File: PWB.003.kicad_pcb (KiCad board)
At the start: 2 copper layers, 61 x 31.5 mm, 58 parts, among them J1 USB_C_Receptacle_PowerOnly_6P, J2 XT30PW-F, J3 XT30PW-M, J4 BAT, J5 Conn_01x04_Pin, J6 Conn_01x05_Pin, Q1 IRLML6402TR, Q2 IRLML6402TR, Q3 2N7002, Q4 IRLML6402TR, U1 TPS63070RNMR, U2 BQ24073RGT

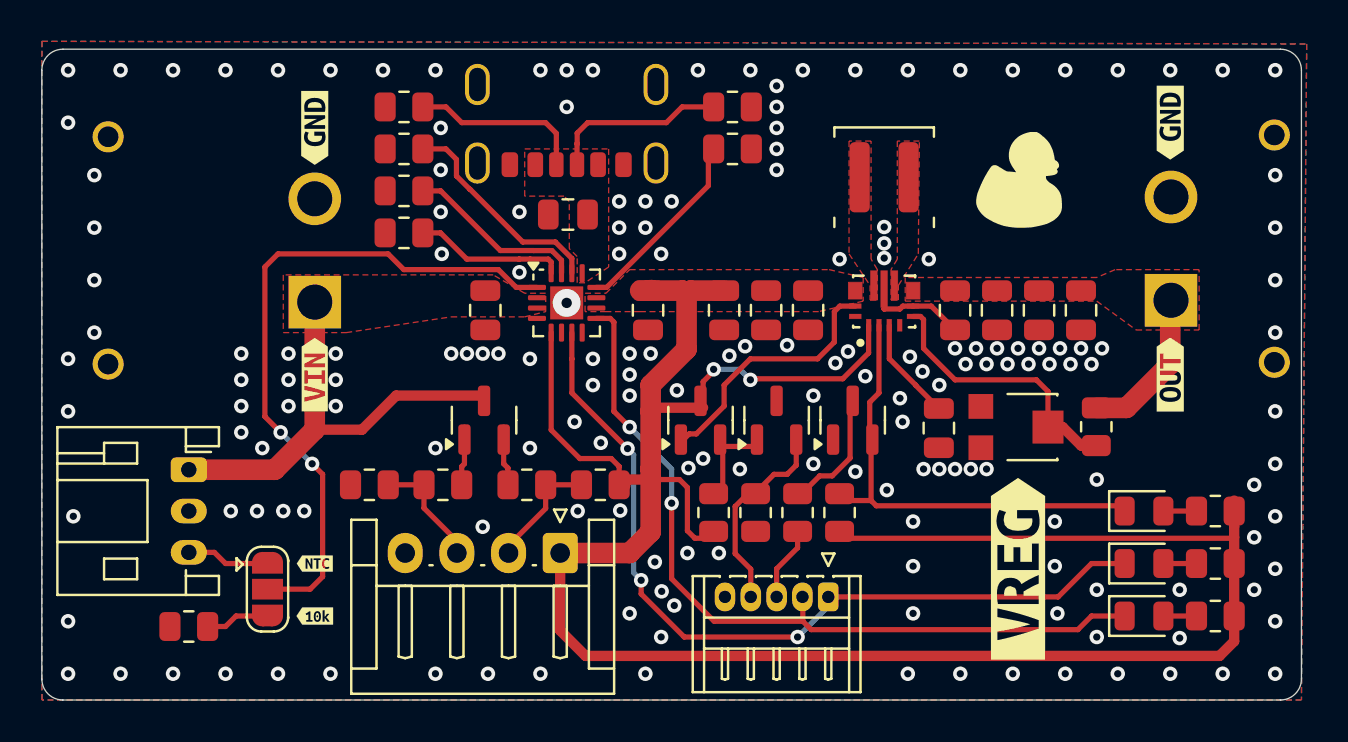
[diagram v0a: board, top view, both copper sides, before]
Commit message: Improved PCB
- Added 10k resistor on control inputs TPS63070
- Changed layout of inductor and filtering capacitors
- added legend on bottom layer
- updated DRC
- validated design on JLCDFM
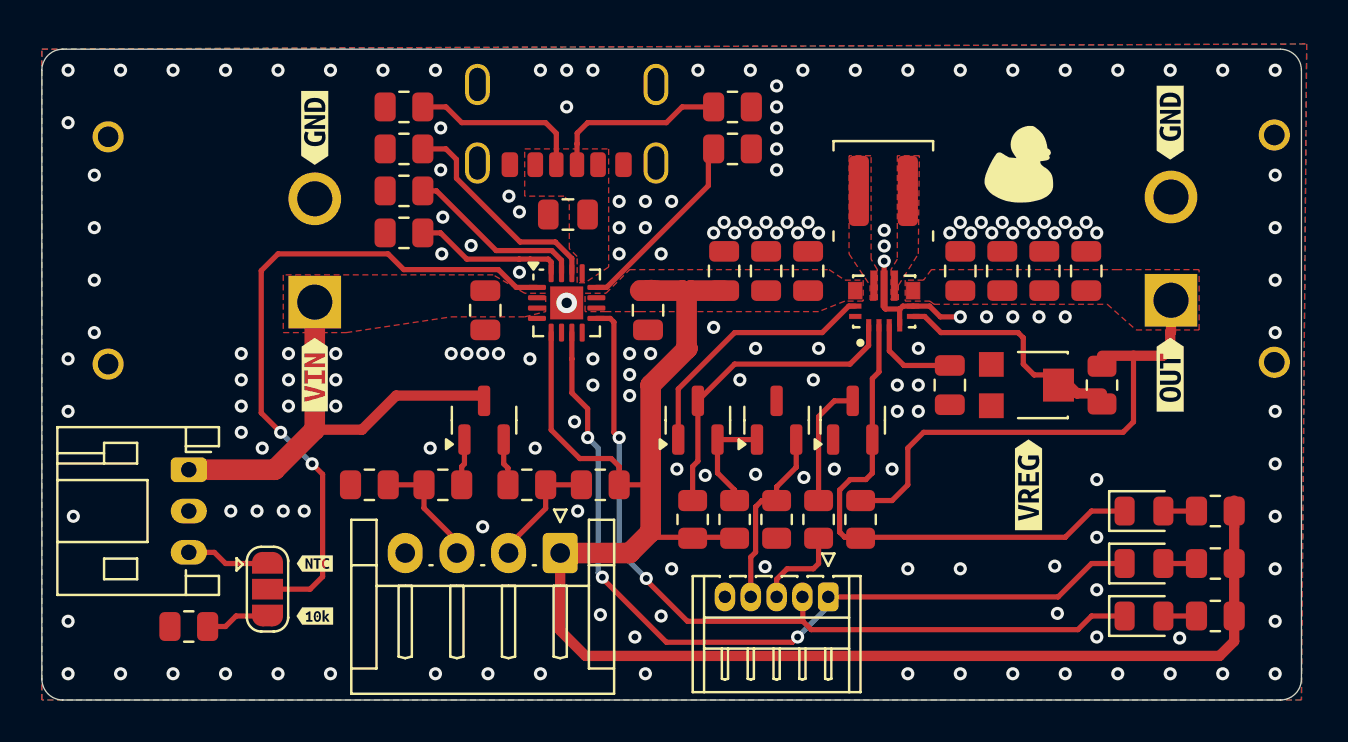
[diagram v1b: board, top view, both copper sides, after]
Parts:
- removed the kibuzzard-8 at (145.8, 112.5)
- added R13: 10k, Resistor_SMD:R_0805_2012Metric, F.Cu at (130.0, 110.1)
- added kibuzzard-678D6AC8: G***, kibuzzard-678D6AC8, B.Cu at (134.1, 111.3)
- added kibuzzard-678D6ACE: G***, kibuzzard-678D6ACE, B.Cu at (132.9, 111.3)
- added kibuzzard-678D6AD4: G***, kibuzzard-678D6AD4, B.Cu at (131.6, 111.0)
- added kibuzzard-678D6AE1: G***, kibuzzard-678D6AE1, B.Cu at (135.4, 111.0)
- added kibuzzard-678D6AE6: G***, kibuzzard-678D6AE6, B.Cu at (136.7, 110.1)
- added kibuzzard-678D6B1B: G***, kibuzzard-678D6B1B, B.Cu at (123.7, 108.8)
- added kibuzzard-678D6B21: G***, kibuzzard-678D6B21, B.Cu at (121.1, 108.0)
- added kibuzzard-678D6B26: G***, kibuzzard-678D6B26, B.Cu at (118.6, 108.5)
- added kibuzzard-678D6B2C: G***, kibuzzard-678D6B2C, B.Cu at (116.1, 109.1)
- added kibuzzard-678D6B8A: G***, kibuzzard-678D6B8A, B.Cu at (102.9, 107.7)
- added kibuzzard-678D6B93: G***, kibuzzard-678D6B93, B.Cu at (102.9, 109.7)
- added kibuzzard-678D6B9C: G***, kibuzzard-678D6B9C, B.Cu at (102.9, 111.8)
- added kibuzzard-7: G***, kibuzzard-678D5D09, F.Cu at (146.3, 108.5)
- moved C11 2.15 mm to (142.5, 103.6)
- moved RV1 2.09 mm to (146.3, 103.6)
- moved R7 2.03 mm to (149.9, 103.6)
- moved C5 1.92 mm to (143.0, 98.1), turned to -90 degrees
- moved C8 1.92 mm to (149.1, 98.1), turned to -90 degrees
- moved C6 1.92 mm to (145.0, 98.1), turned to -90 degrees
- moved C7 1.92 mm to (147.1, 98.1), turned to -90 degrees
- moved C2 1.90 mm to (131.6, 98.1), turned to -90 degrees
- moved C3 1.90 mm to (133.6, 98.1), turned to -90 degrees
- moved C4 1.90 mm to (135.6, 98.1), turned to -90 degrees
- moved R14 1.07 mm to (132.1, 110.1)
- moved R16 1.07 mm to (136.1, 110.1)
- moved R15 1.07 mm to (134.1, 110.1)
- moved R17 1.07 mm to (138.2, 110.1), turned to -90 degrees
- moved G*** 0.76 mm to (145.8, 93.0)
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- renumbered C3 to C10, C4 to C2, C5 to C3, C6 to C4, C7 to C5, C8 to C6, C9 to C7, C10 to C8, C2 to C9, R13 to R14, R14 to R15, R15 to R16, R16 to R17, R17 to R18, R18 to R19, R19 to R20, kibuzzard-7 to kibuzzard-8
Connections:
- Q2 pad 3: VSYS -> Net-(Q2-S)
- R17 pad 1: VSYS -> VOUT
- U1 pad 1: VSYS -> Net-(Q2-S)
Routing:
- net VSYS: track 116.1 -> 80.3 mm, vias 2 -> 0
- net VOUT: track 7.56 -> 24.9 mm
- net Net-(Q2-S): track 0.00 -> 15.3 mm
- net PG: track 22.7 -> 25.7 mm
- net GND: track 4.93 -> 7.03 mm, vias 177 -> 176
- net Net-(U1-FB): track 13.3 -> 11.4 mm
- net PGOOD: track 40.0 -> 40.9 mm
- net CHRG: track 38.9 -> 39.7 mm
- net EN: track 4.46 -> 5.20 mm
- net Net-(J6-Pin_3): track 3.26 -> 3.92 mm
- net Net-(U1-VAUX): track 5.02 -> 4.46 mm
